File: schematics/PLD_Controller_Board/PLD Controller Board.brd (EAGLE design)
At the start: 55.2 x 71.1 mm, 35 parts, among them IC2 ATMEGA328-PU

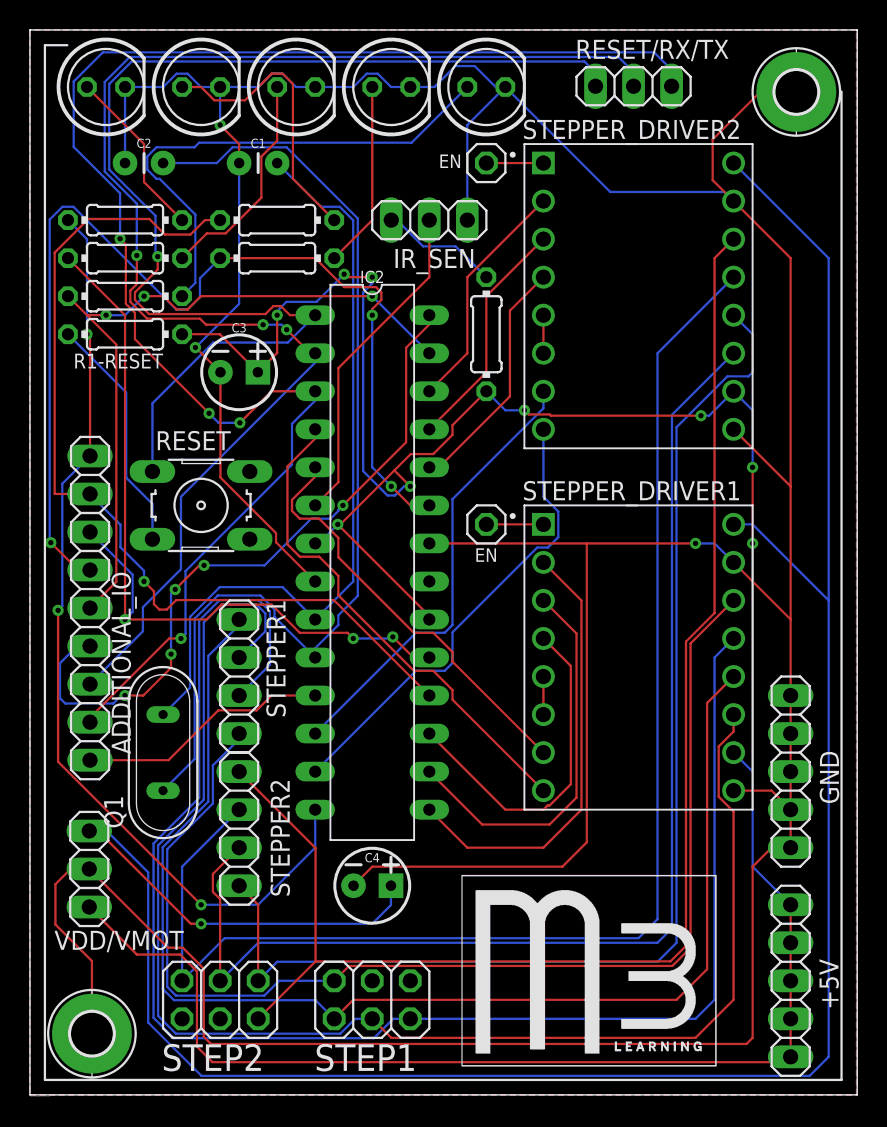
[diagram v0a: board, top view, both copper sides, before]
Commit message: schematic update
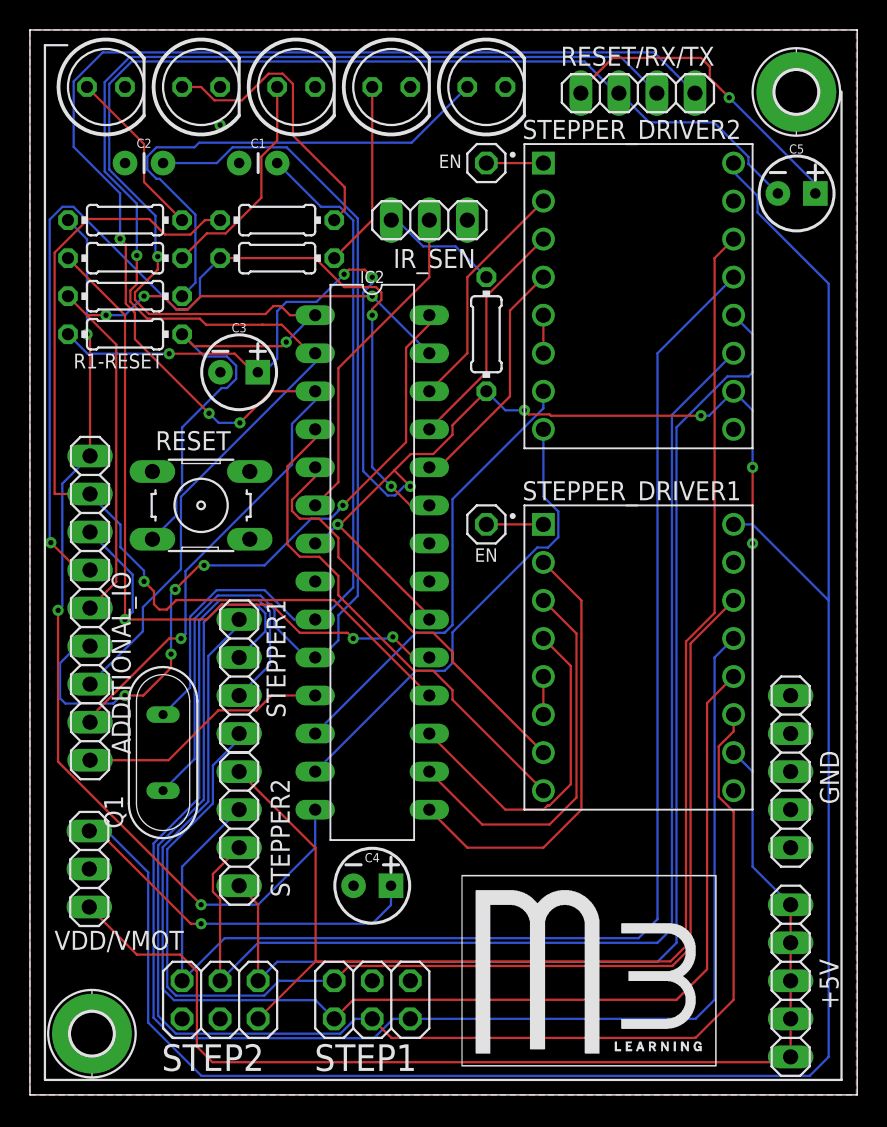
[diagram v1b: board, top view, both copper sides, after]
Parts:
- added C5: 10uF, SparkFun-Capacitors:CPOL-RADIAL-2.5MM-5MM
- RESET/RX/TX: device pinhead:1X03 -> pinhead:1X04
- moved RESET/RX/TX 0.54 mm to (40.6, 66.9)
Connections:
- net +5V: now also R1-RESET.2; no longer R1-RESET.1
- net GND: now also RESET.1
- net N$1: now also C5.2, R1-RESET.1, RESET.3, RESET/RX/TX.2; no longer RESET.1, RESET/RX/TX.1
- net N$38: now also RESET/RX/TX.3; no longer RESET/RX/TX.2
- net N$39: now also RESET/RX/TX.4; no longer RESET/RX/TX.3
- net N$4: now also C5.1, RESET/RX/TX.1; no longer R1-RESET.2, RESET.3
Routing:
- net GND: track 309.5 -> 0.02 mm, vias 3 -> 1
- net N$1: track 81.5 -> 107.2 mm, vias 1 -> 2
- net +5V: track 181.8 -> 189.9 mm
- net N$4: track 16.0 -> 21.3 mm, vias 0 -> 1
- net N$38: track 95.2 -> 96.4 mm, vias 3 -> 1
- net N$39: track 105.2 -> 106.3 mm
- net N$3: track 69.0 -> 69.5 mm
- net N$19: track 19.0 -> 19.6 mm
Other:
- board text removed: "C:/Users/capta/Desktop/m3_newbord.bmp"
